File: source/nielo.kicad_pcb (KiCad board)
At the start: 6 copper layers, 98 x 98 mm, 102 parts, among them J1 TYPE-C-31-M-12, J2 TYPE-C-31-M-12, J3 PZ254V-12-14P, J5 SM04B-SRSS-TB, J6 SM04B-SRSS-TB, J7 SM04B-SRSS-TB, J8 SM04B-SRSS-TB, Q1 AO3401A, Q2 2N7002, Q3 2N7002, Q4 AO3401A, SW1 Tactile Switch, SW2 Tactile Switch, SW3 Tactile Switch, U1 USBLC6-2SC6Y, U2 SC1556, U3 USBLC6-2SC6Y, U5 AP22653W6-7, U6 SN74AHCT1G125DBVR, U7 SN74AHCT1G125DBVR

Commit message: manufactering files & step files added
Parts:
- removed D1: SS54FSH, nielo:SODFL4725X110N
- R24, R25: value 5k1 -> 10k
- moved FB1 5.47 mm to (128.6, 74.9)
- moved C2 4.67 mm to (130.6, 74.4), turned to -90 degrees
- moved C1 4.61 mm to (126.5, 74.4), turned to -90 degrees
- moved kibuzzard-6AB23AAB 0.59 mm to (209.2, 70.0)
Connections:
- C1 pad 2: Net-(D1-K) -> VBUS_HS
- FB1 pad 1: Net-(D1-K) -> VBUS_HS
- R24 pad 2: GND -> +3V3
- R25 pad 2: GND -> +3V3
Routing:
- net Net-(D1-K): track 3.77 -> 0.00 mm
- net VUSB_HS: track 10.1 -> 7.51 mm
- net +3V3: track 12.3 -> 14.2 mm, vias 8 -> 10
- net GND: track 128.2 -> 126.5 mm, vias 96 -> 94
- net VBUS_HS: track 20.9 -> 21.6 mm

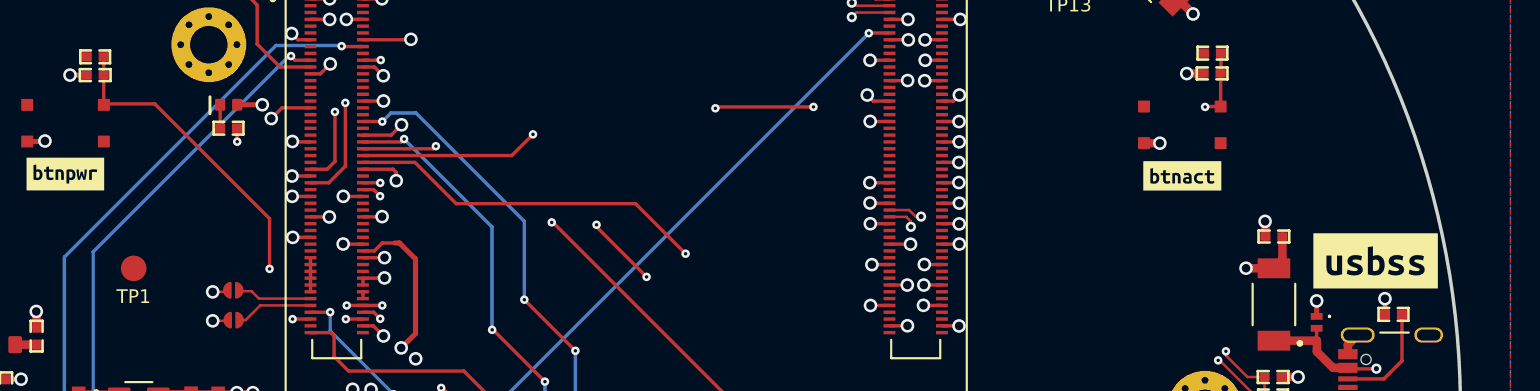
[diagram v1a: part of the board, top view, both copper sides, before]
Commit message: usbss pull-up resistors 10k-->12k
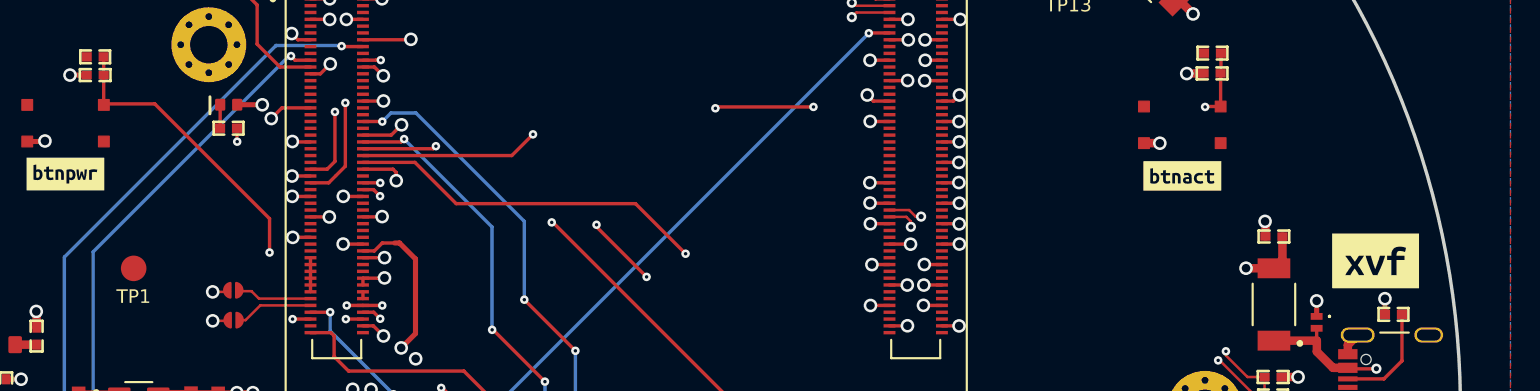
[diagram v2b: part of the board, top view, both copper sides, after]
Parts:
- removed kibuzzard-6AB23AAB: G***, kibuzzard-6AB23AAB
- added kibuzzard-6AB7D9C9: G***, kibuzzard-6AB7D9C9, F.Cu at (209.2, 70.0)
- R24, R25: value 10k -> 12k
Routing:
- net /usbpowerios/pwr_but: track 78.3 -> 77.8 mm
